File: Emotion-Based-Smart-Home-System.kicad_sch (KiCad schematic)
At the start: 10 parts, among them J1 Barrel_Jack, Q1 BC107, U1 HC-SR04, U3 JTE0624D03

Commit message: Current updated schematic
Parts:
- added D3: D, symbol Device:D
- added J2: Barrel_Jack, symbol Connector:Barrel_Jack
- added R1: R_US, symbol Device:R_US
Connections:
- net +9V: now also D3.1 (K)
- net GND: now also U3.11 (VOUT-), U3.2 (VIN-), U3.3 (VIN-), J2.2; no longer U3.16 (COM), U3.9 (COM)
- net at Q1.1 (E): now also R1.2; no longer D1.2 (A)
- net LED_ON: now reaches Q1.2 (B), U2.228 (GPIO13/PWM)
- new net: D3.2 (A), J2.1
- new net: U3.16 (COM), U3.9 (COM)
- new net: D1.2 (A), R1.1
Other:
- note added: "LED Strip"
- note added: "Power"
- note added: "Ultrasonic sensor with Buck Converter"
- title: Emotion-Based-Smart-Home-System  -> Emotion-Adaptive-Smart-Home
- moved on the sheet: C1, C3, D1, D2, J1, Q1, U1, U2, U3

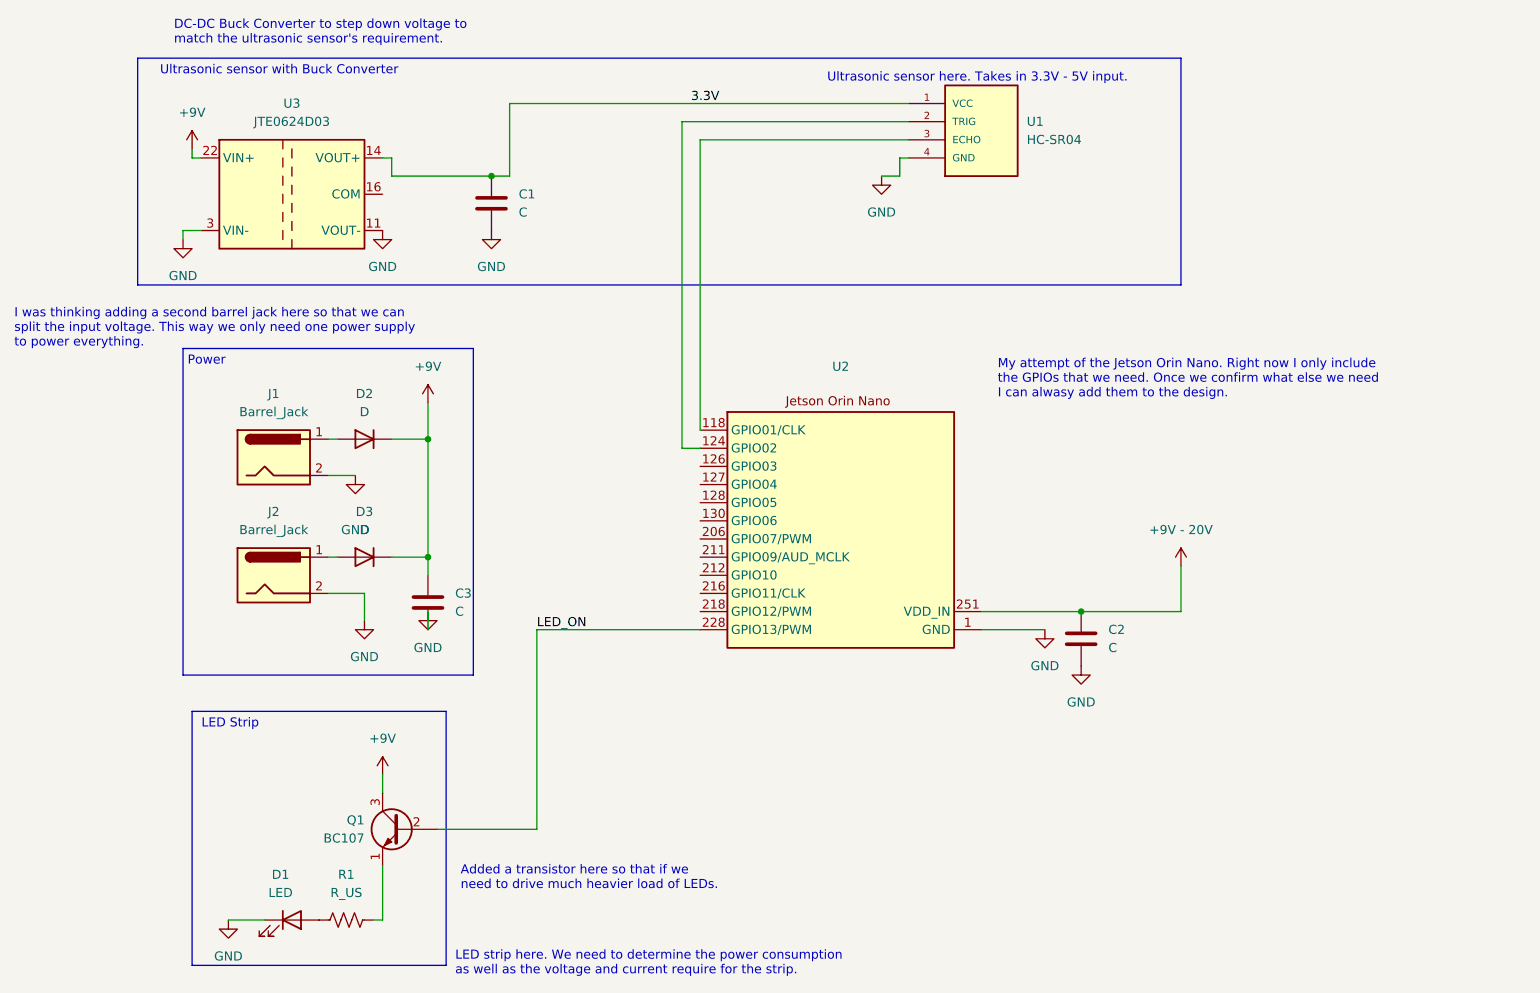
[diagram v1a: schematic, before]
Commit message: Current Schematic
This is the schematic that Luan and Kamal are actively working on
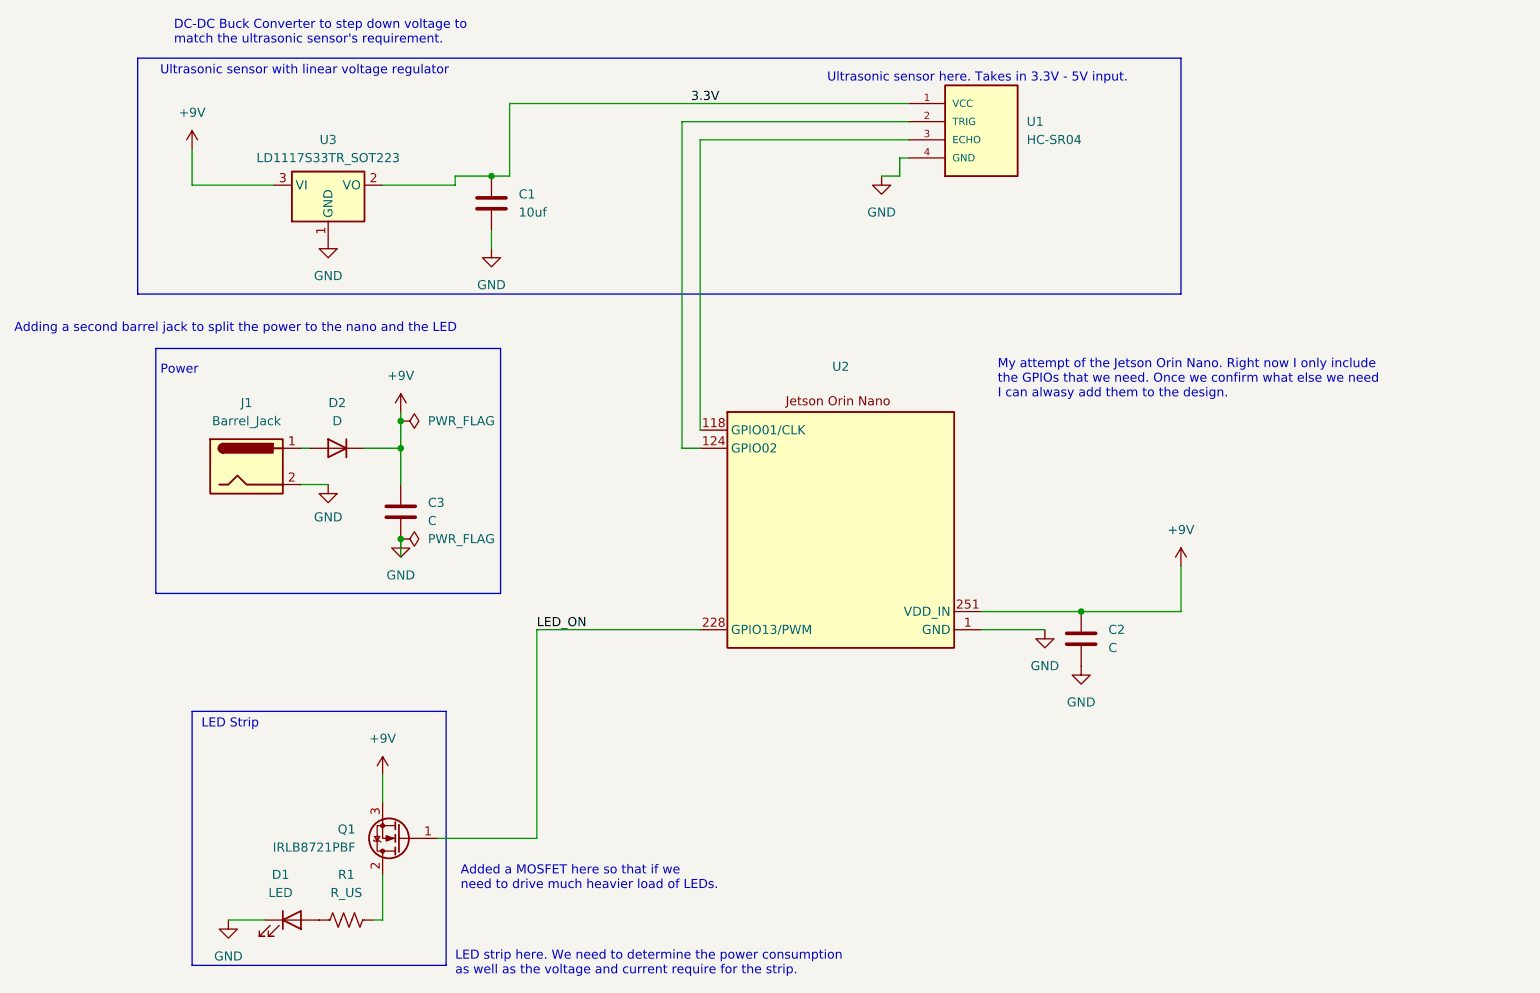
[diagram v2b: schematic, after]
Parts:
- removed D3: D, symbol Device:D
- removed J2: Barrel_Jack, symbol Connector:Barrel_Jack
- removed Q1: BC107, Package_TO_SOT_THT:TO-18-3, symbol Transistor_BJT:BC107
- removed U3: JTE0624D03, Converter_DCDC:Converter_DCDC_XP_POWER_JTExxxxDxx_THT, symbol Converter_DCDC:JTE0624D03
- added Q1: IRLB8721PBF, Package_TO_SOT_THT:TO-220-3_Vertical, symbol Transistor_FET:IRLB8721PBF
- added U3: LD1117S33TR_SOT223, Package_TO_SOT_SMD:SOT-223-3_TabPin2, symbol Regulator_Linear:LD1117S33TR_SOT223
- C1: value C -> 10uf
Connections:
- net +9V - 20V is gone; now on net +9V: C2.1, U2.251 (VDD_IN)
- net +9V: now also Q1.3 (S), U3.3 (VI)
- net 3.3V: now also U3.2 (VO)
- net GND: now also U3.1 (GND)
- net LED_ON: now also Q1.1 (G)
- net at R1.2: now also Q1.2 (D)
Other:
- note added: "Added a MOSFET here so that if we need to drive much heavier load of LEDs."
- note added: "Adding a second barrel jack to split the power to the nano and the LED"
- note added: "Ultrasonic sensor with linear voltage regulator"
- note removed: "Added a transistor here so that if we need to drive much heavier load of LEDs."
- note removed: "I was thinking adding a second barrel jack here so that we can split the input voltage. This way we only need one power supply to power everything."
- note removed: "Ultrasonic sensor with Buck Converter"
- moved on the sheet: C3, D2, J1

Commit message: Updated Kicad design
This is our updated kicad, we still need to add the speaker and finish the camera
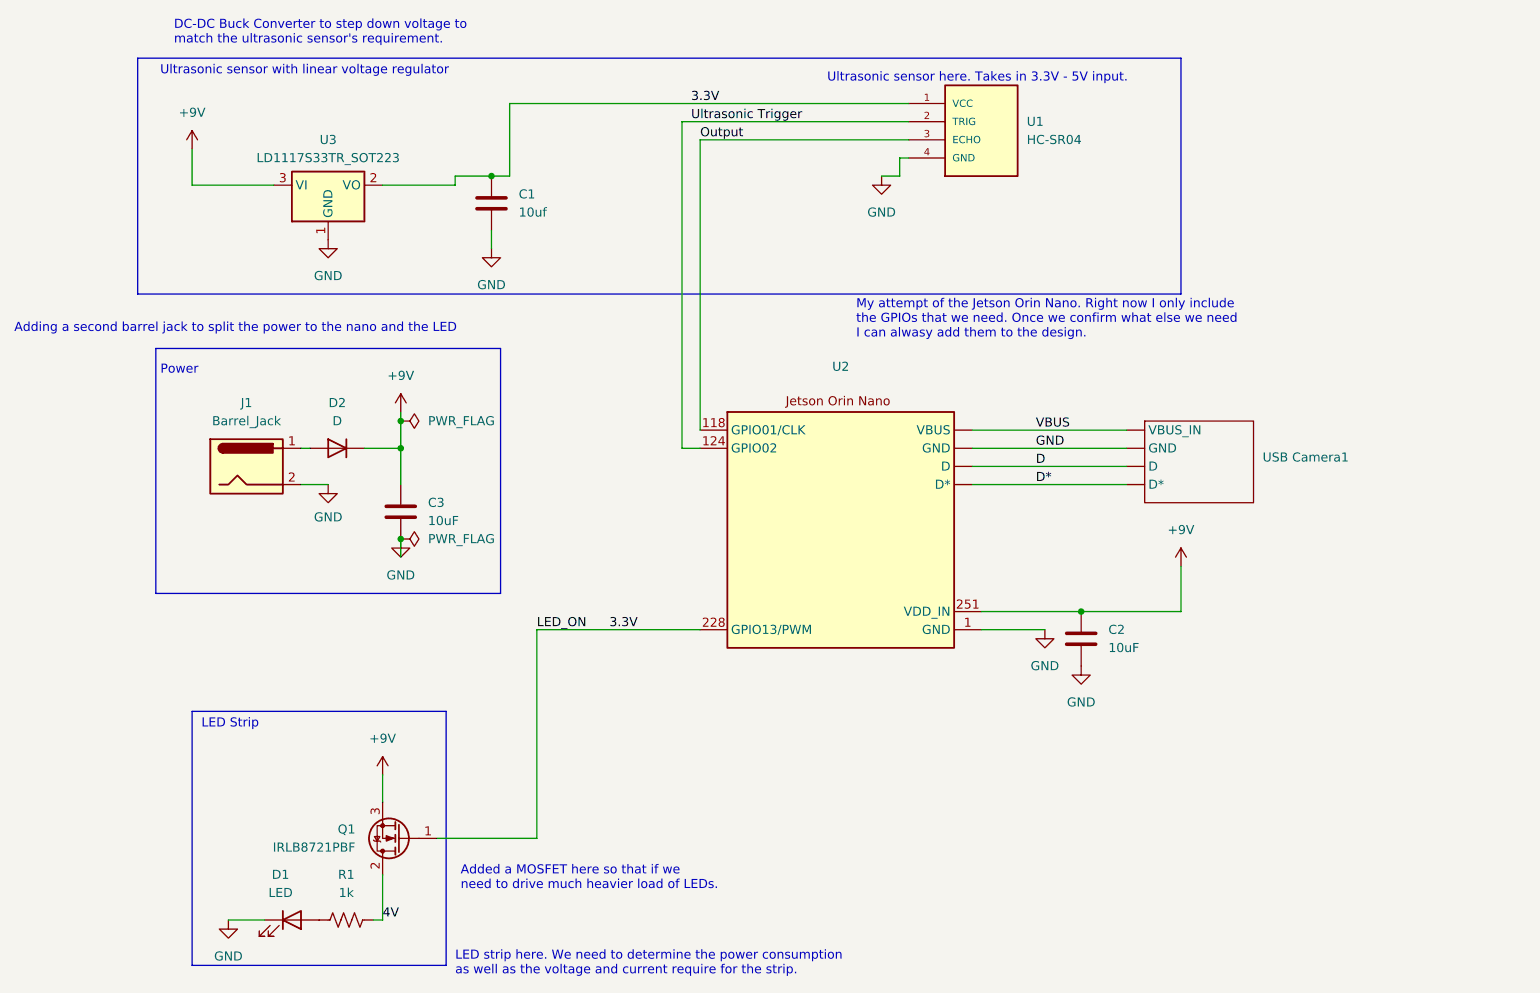
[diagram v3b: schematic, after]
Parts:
- added USB Camera1: ~, symbol CameraModule:USB_Camera
- C2, C3: value C -> 10uF
- R1: value R_US -> 1k
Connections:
- net LED_ON is gone; now on net 3.3V: Q1.1 (G), U2.228 (GPIO13/PWM)
- net GND: now also U2. (VBUS), USB Camera1. (VBUS_IN)
- net Ultrasonic Trigger: now reaches U1.2 (TRIG), U2.124 (GPIO02)
- net Output: now reaches U1.3 (ECHO), U2.118 (GPIO01/CLK)
- net 4V: now reaches Q1.2 (D), R1.2
- new net D: U2. (VBUS), USB Camera1. (VBUS_IN)
- new net D*: U2. (VBUS), USB Camera1. (VBUS_IN)
- new net VBUS: U2. (VBUS), USB Camera1. (VBUS_IN)
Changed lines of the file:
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@@
+	(wire
+		(pts
+			(xy 184.15 78.74) (xy 205.74 78.74)
+		)
+		(stroke
+			(width 0)
+			(type default)
+		)
+	)
 	(wire
 		(pts
@@
 	(wire
 		(pts
+			(xy 184.15 83.82) (xy 205.74 83.82)
+		)
+		(stroke
+			(width 0)
+			(type default)
+		)
+	)
+	(wire
+		(pts
 			(xy 143.51 33.02) (xy 143.51 78.74)
 		)
@@
 	(wire
 		(pts
+			(xy 184.15 76.2) (xy 205.74 76.2)
+		)
+		(stroke
+			(width 0)
+			(type default)
+		)
+	)
+	(wire
+		(pts
 			(xy 109.22 133.35) (xy 123.19 133.35)
 		)
@@
 		(pts
 			(xy 185.42 104.14) (xy 194.31 104.14)
+		)
+		(stroke
+			(width 0)
+			(type default)
+		)
+	)
+	(wire
+		(pts
+			(xy 184.15 81.28) (xy 205.74 81.28)
 		)
 		(stroke
@@
 	(text "My attempt of the Jetson Orin Nano. Right now I only include\nthe GPIOs that we need. Once we confirm what else we need\nI can alwasy add them to the design."
 		(exclude_from_sim no)
-		(at 187.706 69.088 0)
+		(at 167.894 60.706 0)
 		(effects
 			(font
@@
 		)
 	)
+	(label "Ultrasonic Trigger"
+		(at 144.78 33.02 0)
+		(fields_autoplaced yes)
+		(effects
+			(font
+				(size 1.27 1.27)
+			)
+			(justify left bottom)
+		)
+	)
+	(label "D"
+		(at 193.04 81.28 0)
+		(fields_autoplaced yes)
+		(effects
+			(font
+				(size 1.27 1.27)
+			)
+			(justify left bottom)
+		)
+	)
+	(label "3.3V"
+		(at 133.35 104.14 0)
+		(fields_autoplaced yes)
+		(effects
+			(font
+				(size 1.27 1.27)
+			)
+			(justify left bottom)
+		)
+	)
+	(label "GND"
+		(at 193.04 78.74 0)
+		(fields_autoplaced yes)
+		(effects
+			(font
+				(size 1.27 1.27)
+			)
+			(justify left bottom)
+		)
+	)
 	(label "3.3V"
 		(at 144.78 30.48 0)
+		(fields_autoplaced yes)
+		(effects
+			(font
+				(size 1.27 1.27)
+			)
+			(justify left bottom)
+		)
+	)
+	(label "VBUS"
+		(at 193.04 76.2 0)
+		(fields_autoplaced yes)
+		(effects
+			(font
+				(size 1.27 1.27)
+			)
+			(justify left bottom)
+		)
+	)
+	(label "Output"
+		(at 146.05 35.56 0)
+		(fields_autoplaced yes)
+		(effects
+			(font
+				(size 1.27 1.27)
+			)
+			(justify left bottom)
+		)
+	)
+	(label "D*"
+		(at 193.04 83.82 0)
+		(fields_autoplaced yes)
+		(effects
+			(font
+				(size 1.27 1.27)
+			)
+			(justify left bottom)
+		)
+	)
+	(label "4V"
+		(at 101.6 144.78 0)
 		(fields_autoplaced yes)
 		(effects
@@
 			)
 		)
-		(property "Value" "C"
+		(property "Value" "10uF"
 			(at 203.2 106.6799 0)
 			(effects
@@
 	)
 	(symbol
+		(lib_id "CameraModule:USB_Camera")
+		(at 215.9 80.01 0)
+		(unit 1)
+		(exclude_from_sim no)
+		(in_bom yes)
+		(on_board yes)
+		(dnp no)
+		(fields_autoplaced yes)
+		(property "Reference" "USB Camera1"
+			(at 224.79 80.0099 0)
+			(effects
+				(font
+					(size 1.27 1.27)
+				)
+				(justify left)
+			)
+		)
+		(property "Value" "~"
+			(at 224.79 81.915 0)
+			(effects
+				(font
+					(size 1.27 1.27)
+				)
+				(justify left)
+			)
+		)
+		(property "Footprint" ""
+			(at 215.9 80.01 0)
+			(effects
+				(font
+					(size 1.27 1.27)
+				)
+				(hide yes)
+			)
+		)
+		(property "Datasheet" ""
+			(at 215.9 80.01 0)
+			(effects
+				(font
+					(size 1.27 1.27)
+				)
+				(hide yes)
+			)
+		)
+		(property "Description" ""
+			(at 215.9 80.01 0)
+			(effects
+				(font
+					(size 1.27 1.27)
+				)
+				(hide yes)
+			)
+		)
+		(pin ""
+		)
+		(pin ""
+		)
+		(pin ""
+		)
+		(pin ""
+		)
+		(instances
+			(project ""
+				(path "/912fe9f9-2759-4805-8af5-3cb819096563"
+					(reference "USB Camera1")
+					(unit 1)
+				)
+			)
+		)
+	)
+	(symbol
 		(lib_id "power:GND")
 		(at 93.98 49.53 0)
@@
 			)
 		)
-		(property "Value" "C"
+		(property "Value" "10uF"
 			(at 107.95 88.8999 0)
 			(effects
@@
 			)
 		)
-		(property "Value" "R_US"
+		(property "Value" "1k"
 			(at 96.52 140.97 90)
 			(effects
@@
 		(pin "124"
 		)
-		(instances
+		(pin ""
+		)
+		(pin ""
+		)
+		(pin ""
+		)
+		(pin ""
+		)
+		(instances

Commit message: Updated again
Fixed an error and made the GND on the USB camera passive
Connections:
- net 3.3V: no longer Q1.1 (G), U2.228 (GPIO13/PWM)
- new net LED_ON 3.3V: Q1.1 (G), U2.228 (GPIO13/PWM)

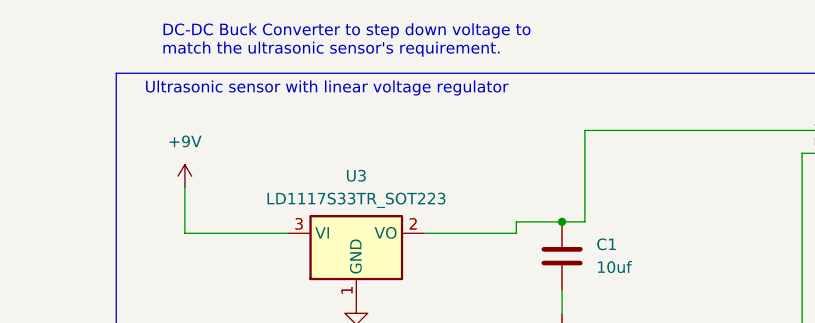
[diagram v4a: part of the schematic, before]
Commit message: Entire design folder
We had to move this into it's own seperate file to get the PCB design to work. Will fix names later
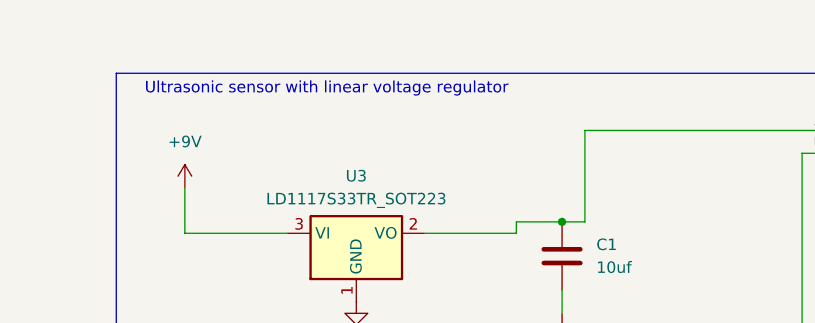
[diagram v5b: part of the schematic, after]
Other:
- note removed: "DC-DC Buck Converter to step down voltage to match the ultrasonic sensor's requirement."
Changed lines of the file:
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@@
-		)
-	)
-	(text "DC-DC Buck Converter to step down voltage to \nmatch the ultrasonic sensor's requirement."
-		(exclude_from_sim no)
-		(at 72.39 20.574 0)
-		(effects
-			(font
-				(size 1.27 1.27)
-			)
-			(justify left)
 		)
 	)
